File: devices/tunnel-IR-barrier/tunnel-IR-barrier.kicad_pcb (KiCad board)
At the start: 2 copper layers, 10 x 42 mm, 21 parts, among them J1 JST SH, J2 JST SH, J4 JST SH, Q1 Q_NMOS_GSD, Q2 Q_NMOS_GSD, Q3 Q_NMOS_GSD, U1 GP2S700HCP, U2 ATtiny204-SS, U3 GP2S700HCP, U4 GP2S700HCP

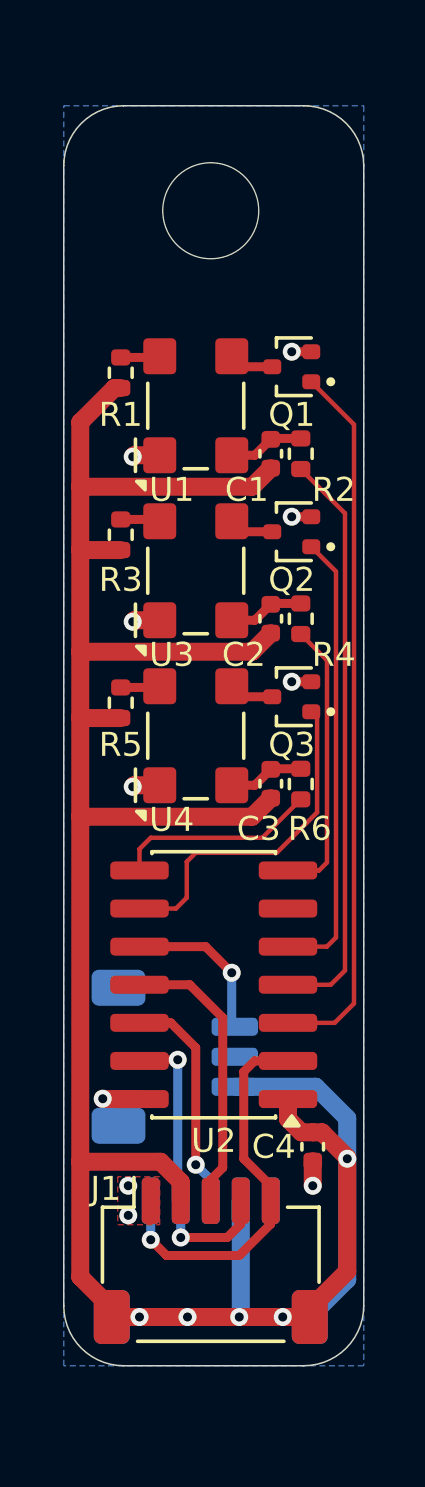
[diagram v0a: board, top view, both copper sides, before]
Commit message: Update IR barrier for easier firmware implementation
Uses a common readout circuitry, and a high-side switch to not have to switch pin direction with interupts
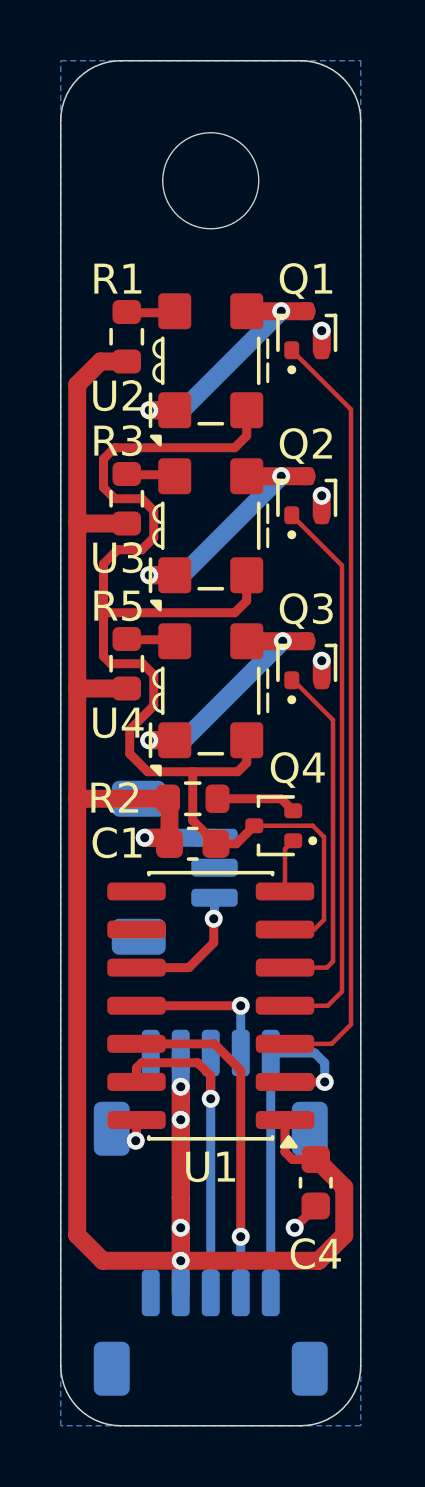
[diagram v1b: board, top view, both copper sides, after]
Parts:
- removed C2, C3: 10n, Capacitor_SMD:C_0402_1005Metric
- removed R4, R6: 220, Resistor_SMD:R_0402_1005Metric
- added Q4: Q_NMOS_GDS, Package_TO_SOT_SMD:SOT-416, F.Cu at (152.6, 74.0)
- added REF**: OSHW-Logo_7.5x8mm_SilkScreen, Symbol:OSHW-Logo_7.5x8mm_SilkScreen, B.Cu at (150.5, 60.0)
- added kibuzzard-6A229D11: G***, kibuzzard-6A229D11, B.Cu at (150.5, 87.3)
- added kibuzzard-6A229D47: G***, kibuzzard-6A229D47, B.Cu at (150.5, 79.3)
- added kibuzzard-6A229D6B: G***, kibuzzard-6A229D6B, B.Cu at (153.0, 75.4)
- added kibuzzard-6A22A01A: G***, kibuzzard-6A22A01A, B.Cu at (150.5, 68.0)
- C1: value 10n -> 2n2; footprint Capacitor_SMD:C_0402_1005Metric -> Capacitor_SMD:C_0603_1608Metric
- C4: footprint Capacitor_SMD:C_0402_1005Metric -> Capacitor_SMD:C_0603_1608Metric
- J1: footprint Connector_JST:JST_SH_SM05B-SRSS-TB_1x05-1MP_P1.00mm_Horizontal -> Connector_JST:JST_SH_BM05B-SRSS-TB_1x05-1MP_P1.00mm_Vertical; moved to B.Cu
- J2: footprint Connector_JST:JST_SH_SM05B-SRSS-TB_1x05-1MP_P1.00mm_Horizontal -> Connector_JST:JST_SH_BM05B-SRSS-TB_1x05-1MP_P1.00mm_Vertical
- J4: footprint Connector_JST:JST_SH_SM03B-SRSS-TB_1x03-1MP_P1.00mm_Horizontal -> Connector_JST:JST_SH_BM03B-SRSS-TB_1x03-1MP_P1.00mm_Vertical
- R1, R3, R5: value 100 -> 470; footprint Resistor_SMD:R_0402_1005Metric -> Resistor_SMD:R_0603_1608Metric
- R2: value 220 -> 860; footprint Resistor_SMD:R_0402_1005Metric -> Resistor_SMD:R_0603_1608Metric
- moved C1 13.3 mm to (149.9, 74.6), turned to 0 degrees
- moved R2 12.1 mm to (149.9, 73.1), turned to 180 degrees
- moved J4 6.30 mm to (149.3, 75.4), turned to -90 degrees
- moved J1 5.60 mm to (150.5, 82.9)
- moved J2 2.40 mm to (150.5, 90.9), turned to 0 degrees
- moved U2 1.58 mm to (150.5, 58.5)
- moved U3 1.58 mm to (150.5, 64.0)
- moved U4 1.58 mm to (150.5, 69.5)
- moved R5 1.32 mm to (147.7, 68.6)
- moved Q1 1.30 mm to (153.7, 57.5), turned to 90 degrees
- moved Q2 1.30 mm to (153.7, 63.0), turned to 90 degrees
- moved Q3 1.30 mm to (153.7, 68.5), turned to 90 degrees
- moved R1 1.22 mm to (147.7, 57.7)
- moved R3 1.22 mm to (147.7, 63.1)
- moved C4 1.20 mm to (154.0, 85.9)
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- renumbered U2 to U1, U1 to U2
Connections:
- C1 pad 2: /IR_C0 -> /IR_OUT
- J1 pad 3: /DIN -> /CLK
- J1 pad 4: /CLK -> /DIN
- J1 pad MP: +3V3 -> GND
- J2 pad 3: /DOUT -> /CLK
- J2 pad 4: /CLK -> /DOUT
- J2 pad MP: +3V3 -> GND
- R2 pad 1: /IR_C0 -> Net-(Q4-D)
- R2 pad 2: /IR_OUT0 -> +3V3
- U1 pad 4: /IR_OUT0 -> /IR_ON1
- U1 pad 5: /IR_ON1 -> /IR_ON2
- U1 pad 6: unconnected-(U2-PB3-Pad6) -> /IR_OUT
- U1 pad 7: /IR_OUT1 -> /DISCHARGE
- U1 pad 8: /IR_OUT2 -> unconnected-(U1-PB1-Pad8)
- U1 pad 9: /IR_ON2 -> unconnected-(U1-PB0-Pad9)
- U2 pad 1: GND -> /IR_K0
- U2 pad 2: /IR_C0 -> /IR_OUT
- U3 pad 1: GND -> /IR_K1
- U3 pad 2: /IR_C1 -> /IR_OUT
- U4 pad 1: GND -> /IR_K2
- U4 pad 2: /IR_C2 -> /IR_OUT
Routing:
- net /IR_OUT: track 0.00 -> 41.5 mm
- net +3V3: track 96.3 -> 70.0 mm
- net /IR_OUT0: track 19.4 -> 0.00 mm
- net /IR_OUT1: track 9.39 -> 0.00 mm
- net /IR_K2: track 1.49 -> 8.67 mm, vias 0 -> 2
- net /IR_K1: track 1.49 -> 8.62 mm, vias 0 -> 2
- net /IR_K0: track 1.49 -> 8.62 mm, vias 0 -> 2
- net /IR_OUT2: track 6.78 -> 0.00 mm
- net /DIN: track 9.50 -> 5.05 mm, vias 0 -> 1
- net /DOUT: track 7.53 -> 11.3 mm
- net /IR_ON1: track 15.1 -> 18.7 mm
- net GND: track 6.76 -> 3.67 mm, vias 10 -> 5
- net Net-(Q4-D): track 0.00 -> 2.69 mm
- net /IR_C1: track 2.53 -> 0.00 mm
- net /IR_C0: track 2.53 -> 0.00 mm
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- removed copper zone on F.Cu, net GND
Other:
- board size 10 x 42 mm -> 10 x 45.5 mm

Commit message: !fixup
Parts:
- J1, J2: value JST SH -> JST SH 5
- J4: value JST SH -> JST SH 2
- Q1, Q2, Q3: value Q_NMOS_GSD -> RE1C002UN
- Q4: value Q_NMOS_GDS -> RE1C001ZP
- R2: value 860 -> 820
